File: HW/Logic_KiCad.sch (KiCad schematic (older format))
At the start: 31 parts, among them Q10 Q_NMOS_GSD, Q11 Q_NMOS_GSD, Q3 Q_NMOS_GSD, SW1 SW_SPDT, U1 ESP32-PICO-D4

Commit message: repair footprint of DIP and USB micro, change buttons with higher fretboard
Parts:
- D92: symbol Simulation_SPICE:DIODE -> Device:D
- gave numbers to parts that had none: 2
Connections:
- net V_IN: now also D92.2 (A); no longer D92.1 (A)
- net at SW1.2 (B): now also D92.1 (K); no longer D92.2 (K)
- no-connect marks 15 -> 16
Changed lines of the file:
@@
 Connection ~ 4550 3150
 Wire Wire Line
-	4550 3150 4550 3050
+	4550 3150 4550 3100
 Text GLabel 5950 4750 2    50   Input ~ 0
 RX_ESP
@@
 Text GLabel 9800 2150 0    50   Input ~ 0
 V_LED_1
-Wire Wire Line
-	9950 2150 9800 2150
 $Sheet
 S 600  3250 1000 400
@@
 Text GLabel 9750 900  0    50   Input ~ 0
 V_LED_1
-Wire Wire Line
-	9750 900  9950 900
-Wire Wire Line
-	9750 1050 9950 1050
 Text GLabel 7500 900  0    50   Input ~ 0
 V_LED_1
@@
 	7500 750  7800 750
 Wire Wire Line
-	7500 900  7800 900
-Wire Wire Line
-	7500 1050 7800 1050
+	7500 900  7550 900
 Text GLabel 5950 5350 2    50   Input ~ 0
 ZAPINANI_1_CAST_LED
@@
 	5800 7350 5800 7150
 Wire Wire Line
-	7800 1200 7500 1200
-Wire Wire Line
-	9950 1200 9750 1200
+	7800 1200 7750 1200
 Text GLabel 7500 1200 0    50   Input ~ 0
 V_LED_3
@@
 $EndComp
 $Comp
-L Simulation_SPICE:DIODE D92
+L Device:D D92
 U 1 1 600E85D1
 P 4600 2300
@@
 F 7 "0;0;180" H 4600 2300 50  0001 C CNN "JLCPCB_CORRECTION"
 	1    4600 2300
-	1    0    0    1
+	-1   0    0    -1
 $EndComp
 Wire Wire Line
@@
 	8250 5350 8250 5450
 Wire Wire Line
-	9000 5250 9000 5450
+	9000 5250 9000 5350
 Wire Wire Line
 	8100 5900 8250 5900
@@
 Connection ~ 9000 5900
 $Comp
-L Switch:SW_SPST SW?
+L Switch:SW_SPST SW13
 U 1 1 603F7020
 P 2300 2800
-F 0 "SW?" H 2300 3035 50  0000 C CNN
+F 0 "SW13" H 2300 3035 50  0000 C CNN
 F 1 "SW_SPST" H 2300 2944 50  0000 C CNN
 F 2 "my_library:DIP1x1" H 2300 2800 50  0001 C CNN
@@
 	2100 2800 1950 2800
 $Comp
-L power:GND #PWR?
+L power:GND #PWR0224
 U 1 1 603FDE4B
 P 2750 2800
-F 0 "#PWR?" H 2750 2550 50  0001 C CNN
+F 0 "#PWR0224" H 2750 2550 50  0001 C CNN
 F 1 "GND" H 2755 2627 50  0000 C CNN
 F 2 "" H 2750 2800 50  0001 C CNN
@@
 	2750 2800 2500 2800
 $Comp
-L Switch:SW_SPST SW?
+L Switch:SW_SPST SW14
 U 1 1 604089F0
 P 2850 2350
-F 0 "SW?" H 2850 2585 50  0000 C CNN
+F 0 "SW14" H 2850 2585 50  0000 C CNN
 F 1 "SW_SPST" H 2850 2494 50  0000 C CNN
 F 2 "my_library:DIP1x1" H 2850 2350 50  0001 C CNN
@@
 	2650 2350 2500 2350
 $Comp
-L power:GND #PWR?
+L power:GND #PWR0225
 U 1 1 604089F8
 P 3300 2350
-F 0 "#PWR?" H 3300 2100 50  0001 C CNN
+F 0 "#PWR0225" H 3300 2100 50  0001 C CNN
 F 1 "GND" H 3305 2177 50  0000 C CNN
 F 2 "" H 3300 2350 50  0001 C CNN
@@
 Wire Wire Line
 	5950 4950 5450 4950
+NoConn ~ 3850 6150
+$Comp
+L power:PWR_FLAG #FLG0101
+U 1 1 605181B3
+P 4550 3100
+F 0 "#FLG0101" H 4550 3175 50  0001 C CNN
+F 1 "PWR_FLAG" V 4550 3227 50  0000 L CNN
+F 2 "" H 4550 3100 50  0001 C CNN
+F 3 "~" H 4550 3100 50  0001 C CNN
+	1    4550 3100
+	0    -1   -1   0
+$EndComp
+Connection ~ 4550 3100
+Wire Wire Line
+	4550 3100 4550 3050
+$Comp
+L power:PWR_FLAG #FLG0102
+U 1 1 60519879
+P 9000 5350
+F 0 "#FLG0102" H 9000 5425 50  0001 C CNN
+F 1 "PWR_FLAG" V 9000 5478 50  0000 L CNN
+F 2 "" H 9000 5350 50  0001 C CNN
+F 3 "~" H 9000 5350 50  0001 C CNN
+	1    9000 5350
+	0    1    1    0
+$EndComp
+Connection ~ 9000 5350
+Wire Wire Line
+	9000 5350 9000 5450
+$Comp
+L power:PWR_FLAG #FLG0105
+U 1 1 6051C980
+P 7600 1050
+F 0 "#FLG0105" H 7600 1125 50  0001 C CNN
+F 1 "PWR_FLAG" H 7600 1223 50  0000 C CNN
+F 2 "" H 7600 1050 50  0001 C CNN
+F 3 "~" H 7600 1050 50  0001 C CNN
+	1    7600 1050
+	-1   0    0    1
+$EndComp
+$Comp
+L power:PWR_FLAG #FLG0107
+U 1 1 6051CE63
+P 7750 1200
+F 0 "#FLG0107" H 7750 1275 50  0001 C CNN
+F 1 "PWR_FLAG" H 7750 1373 50  0000 C CNN
+F 2 "" H 7750 1200 50  0001 C CNN
+F 3 "~" H 7750 1200 50  0001 C CNN
+	1    7750 1200
+	-1   0    0    1
+$EndComp
+Connection ~ 7750 1200
+Wire Wire Line
+	7750 1200 7500 1200
+$Comp
+L power:PWR_FLAG #FLG0109
+U 1 1 6051D33A
+P 7550 900
+F 0 "#FLG0109" H 7550 975 50  0001 C CNN
+F 1 "PWR_FLAG" H 7550 1073 50  0000 C CNN
+F 2 "" H 7550 900 50  0001 C CNN
+F 3 "~" H 7550 900 50  0001 C CNN
+	1    7550 900
+	-1   0    0    1
+$EndComp
+Connection ~ 7550 900
+Wire Wire Line
+	7550 900  7800 900
+Wire Wire Line
+	9750 900  9950 900
+Wire Wire Line
+	9750 1200 9950 1200
+Wire Wire Line
+	7500 1050 7600 1050
+Wire Wire Line
+	9800 2150 9950 2150
+Connection ~ 7600 1050
+Wire Wire Line
+	7600 1050 7800 1050
+Wire Wire Line
+	9750 1050 9950 1050
 $EndSCHEMATC

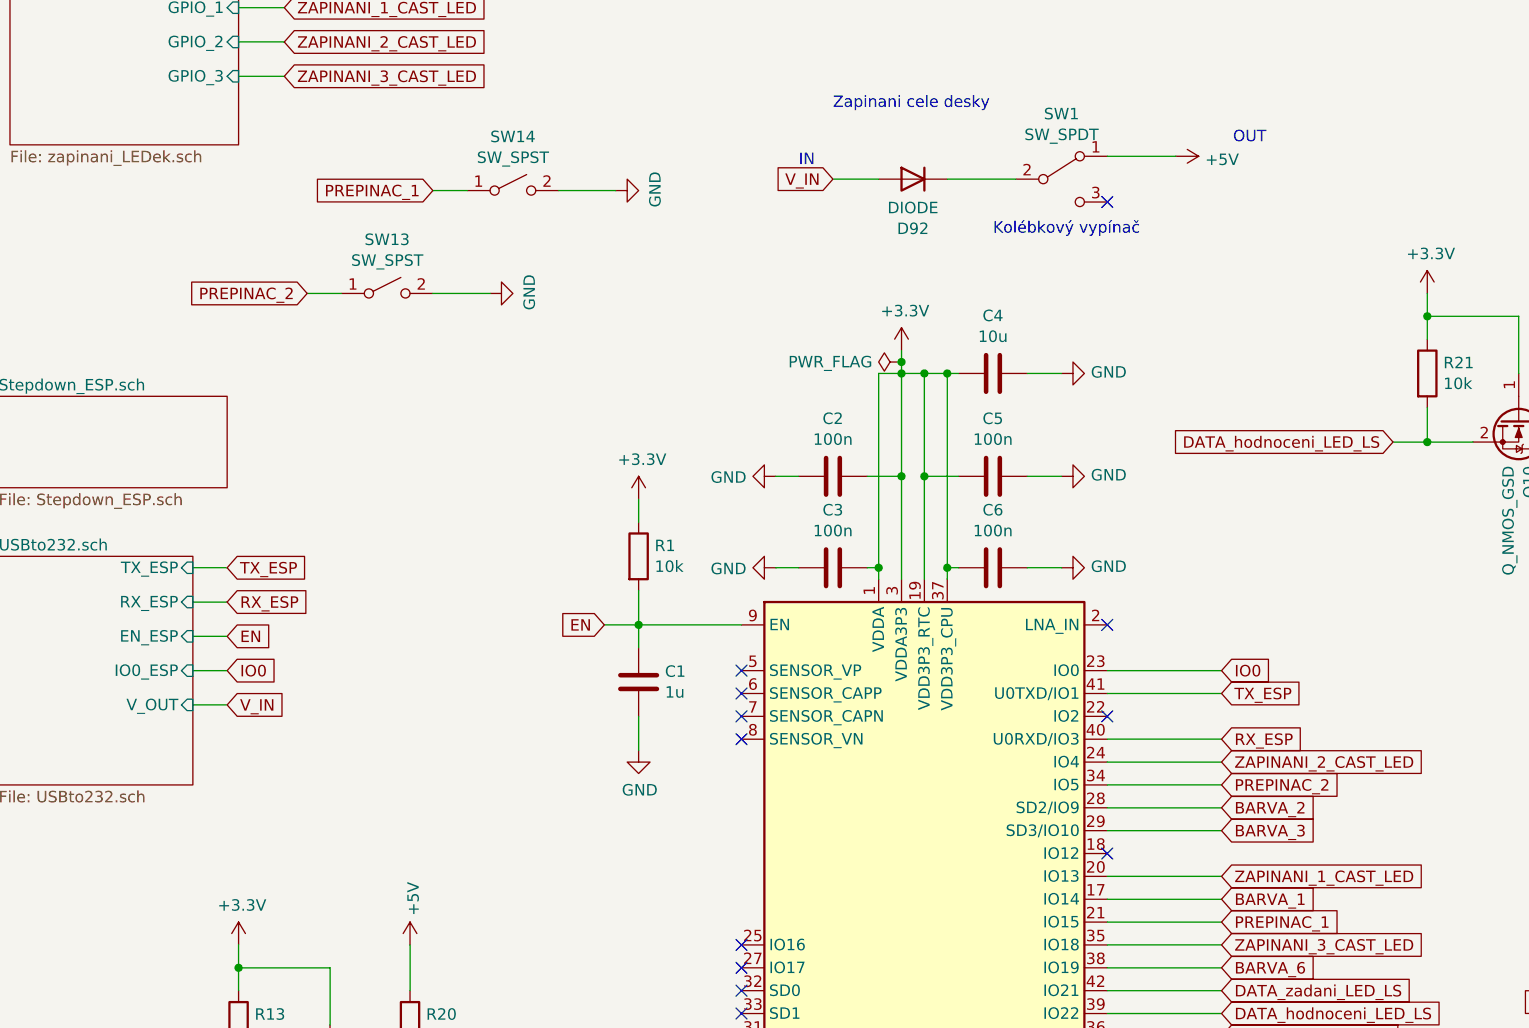
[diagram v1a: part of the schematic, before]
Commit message: change USB footprint, add 3. DIP
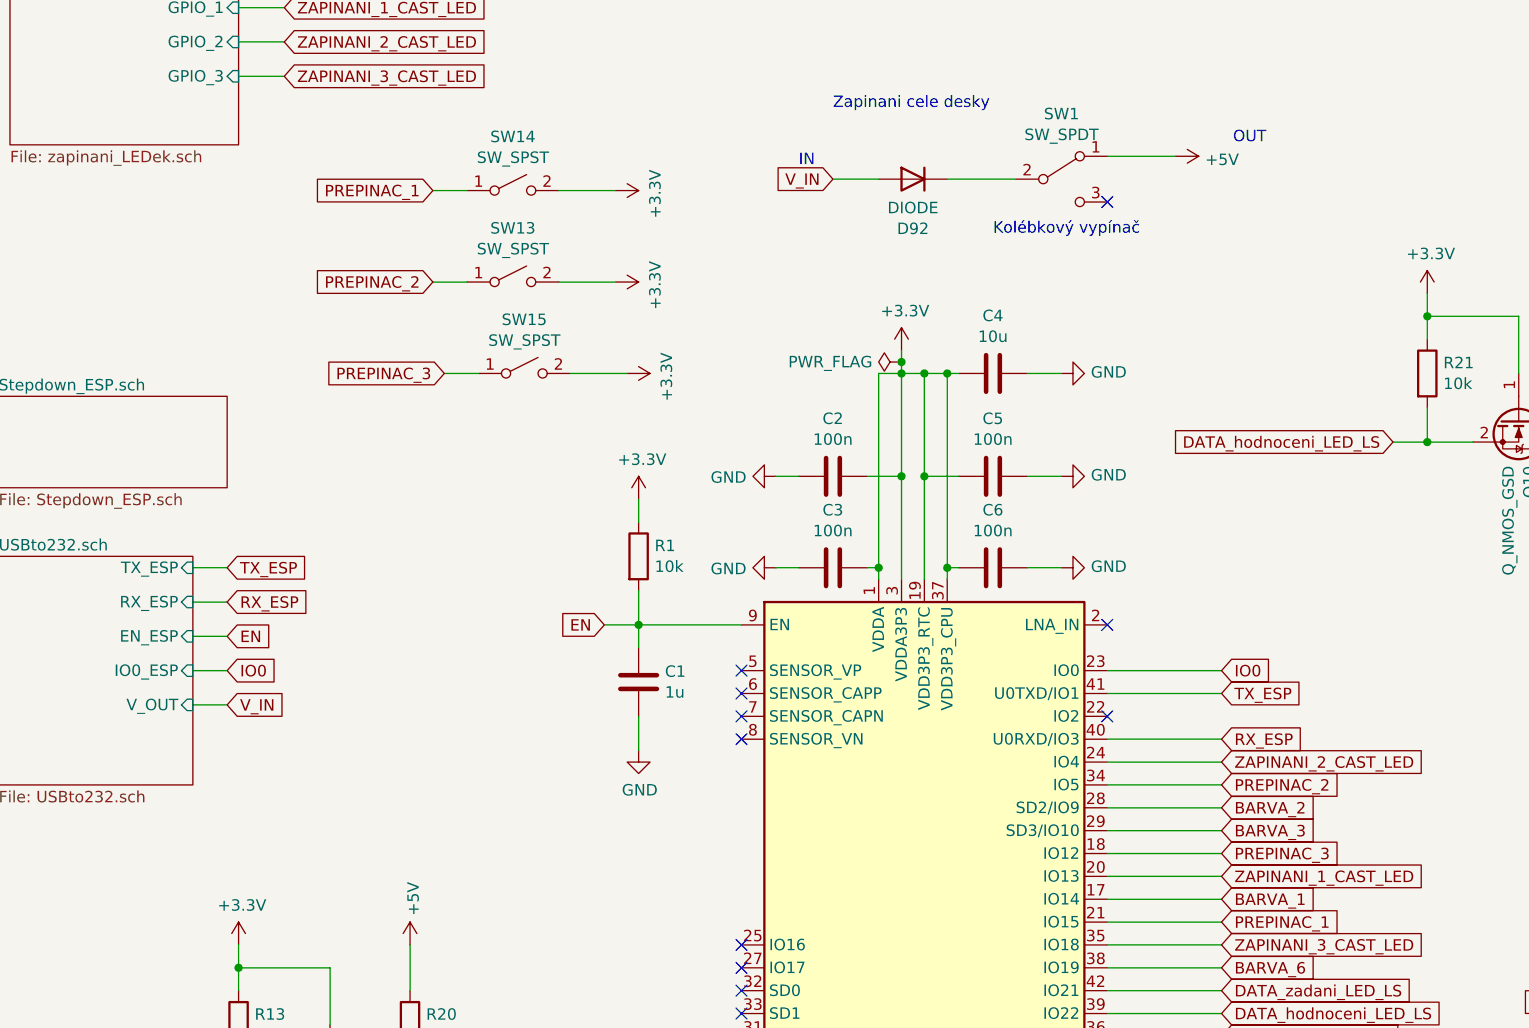
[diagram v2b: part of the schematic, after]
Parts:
- added SW15: SW_SPST, my_library:DIP1x1, symbol Switch:SW_SPST
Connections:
- net +3V3: now also SW13.2 (B), SW14.2 (B), SW15.2 (B)
- net GND: no longer SW13.2 (B), SW14.2 (B)
- net PREPINAC_3: now reaches U1.18 (IO12)
- net PREPINAC_3: now also SW15.1 (A)
- no-connect marks 16 -> 15
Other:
- moved on the sheet: SW13
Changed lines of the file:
@@
 Wire Wire Line
 	5100 4000 5250 4000
-NoConn ~ 5450 5250
 Wire Wire Line
 	5450 6450 5950 6450
@@
 L Switch:SW_SPST SW13
 U 1 1 603F7020
-P 2300 2800
-F 0 "SW13" H 2300 3035 50  0000 C CNN
-F 1 "SW_SPST" H 2300 2944 50  0000 C CNN
-F 2 "my_library:DIP1x1" H 2300 2800 50  0001 C CNN
-F 3 "~" H 2300 2800 50  0001 C CNN
-F 4 "0;0;0" H 2300 2800 50  0001 C CNN "JLCPCB_CORRECTION"
-F 5 "C54948" H 2300 2800 50  0001 C CNN "LCSC"
-	1    2300 2800
-	1    0    0    -1
-$EndComp
-Text GLabel 1950 2800 0    50   Input ~ 0
+P 2850 2750
+F 0 "SW13" H 2850 2985 50  0000 C CNN
+F 1 "SW_SPST" H 2850 2894 50  0000 C CNN
+F 2 "my_library:DIP1x1" H 2850 2750 50  0001 C CNN
+F 3 "~" H 2850 2750 50  0001 C CNN
+F 4 "0;0;0" H 2850 2750 50  0001 C CNN "JLCPCB_CORRECTION"
+F 5 "C54948" H 2850 2750 50  0001 C CNN "LCSC"
+	1    2850 2750
+	1    0    0    -1
+$EndComp
+Text GLabel 2500 2750 0    50   Input ~ 0
 PREPINAC_2
 Wire Wire Line
-	2100 2800 1950 2800
-$Comp
-L power:GND #PWR0224
-U 1 1 603FDE4B
-P 2750 2800
-F 0 "#PWR0224" H 2750 2550 50  0001 C CNN
-F 1 "GND" H 2755 2627 50  0000 C CNN
-F 2 "" H 2750 2800 50  0001 C CNN
-F 3 "" H 2750 2800 50  0001 C CNN
-	1    2750 2800
-	0    -1   -1   0
-$EndComp
-Wire Wire Line
-	2750 2800 2500 2800
+	2650 2750 2500 2750
+Wire Wire Line
+	3300 2750 3050 2750
 $Comp
 L Switch:SW_SPST SW14
@@
 Wire Wire Line
 	2650 2350 2500 2350
-$Comp
-L power:GND #PWR0225
-U 1 1 604089F8
-P 3300 2350
-F 0 "#PWR0225" H 3300 2100 50  0001 C CNN
-F 1 "GND" H 3305 2177 50  0000 C CNN
-F 2 "" H 3300 2350 50  0001 C CNN
-F 3 "" H 3300 2350 50  0001 C CNN
-	1    3300 2350
-	0    -1   -1   0
-$EndComp
 Wire Wire Line
 	3300 2350 3050 2350
@@
 Wire Wire Line
 	9750 1050 9950 1050
+$Comp
+L power:+3.3V #PWR0224
+U 1 1 605155D5
+P 3300 2750
+F 0 "#PWR0224" H 3300 2600 50  0001 C CNN
+F 1 "+3.3V" H 3315 2923 50  0000 C CNN
+F 2 "" H 3300 2750 50  0001 C CNN
+F 3 "" H 3300 2750 50  0001 C CNN
+	1    3300 2750
+	0    1    1    0
+$EndComp
+Text GLabel 5950 5250 2    50   Input ~ 0
+PREPINAC_3
+Wire Wire Line
+	5450 5250 5950 5250
+$Comp
+L Switch:SW_SPST SW15
+U 1 1 60524DA3
+P 2900 3150
+F 0 "SW15" H 2900 3385 50  0000 C CNN
+F 1 "SW_SPST" H 2900 3294 50  0000 C CNN
+F 2 "my_library:DIP1x1" H 2900 3150 50  0001 C CNN
+F 3 "~" H 2900 3150 50  0001 C CNN
+F 4 "0;0;0" H 2900 3150 50  0001 C CNN "JLCPCB_CORRECTION"
+F 5 "C54948" H 2900 3150 50  0001 C CNN "LCSC"
+	1    2900 3150
+	1    0    0    -1
+$EndComp
+Text GLabel 2550 3150 0    50   Input ~ 0
+PREPINAC_3
+Wire Wire Line
+	2700 3150 2550 3150
+Wire Wire Line
+	3350 3150 3100 3150
+$Comp
+L power:+3.3V #PWR0225
+U 1 1 60524DAC
+P 3350 3150
+F 0 "#PWR0225" H 3350 3000 50  0001 C CNN
+F 1 "+3.3V" H 3365 3323 50  0000 C CNN
+F 2 "" H 3350 3150 50  0001 C CNN
+F 3 "" H 3350 3150 50  0001 C CNN
+	1    3350 3150
+	0    1    1    0
+$EndComp
+$Comp
+L power:+3.3V #PWR0229
+U 1 1 6052B776
+P 3300 2350
+F 0 "#PWR0229" H 3300 2200 50  0001 C CNN
+F 1 "+3.3V" H 3315 2523 50  0000 C CNN
+F 2 "" H 3300 2350 50  0001 C CNN
+F 3 "" H 3300 2350 50  0001 C CNN
+	1    3300 2350
+	0    1    1    0
+$EndComp
 $EndSCHEMATC
